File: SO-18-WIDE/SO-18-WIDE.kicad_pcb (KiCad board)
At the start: 2 copper layers, 3 parts

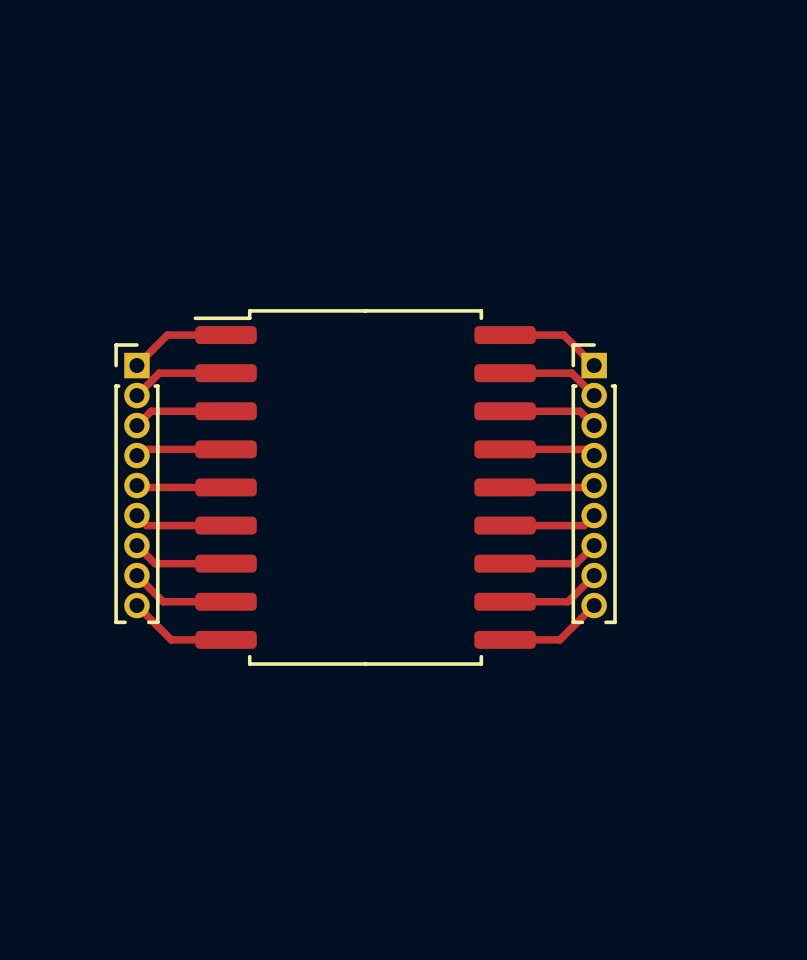
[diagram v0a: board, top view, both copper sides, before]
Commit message: added edge cuts
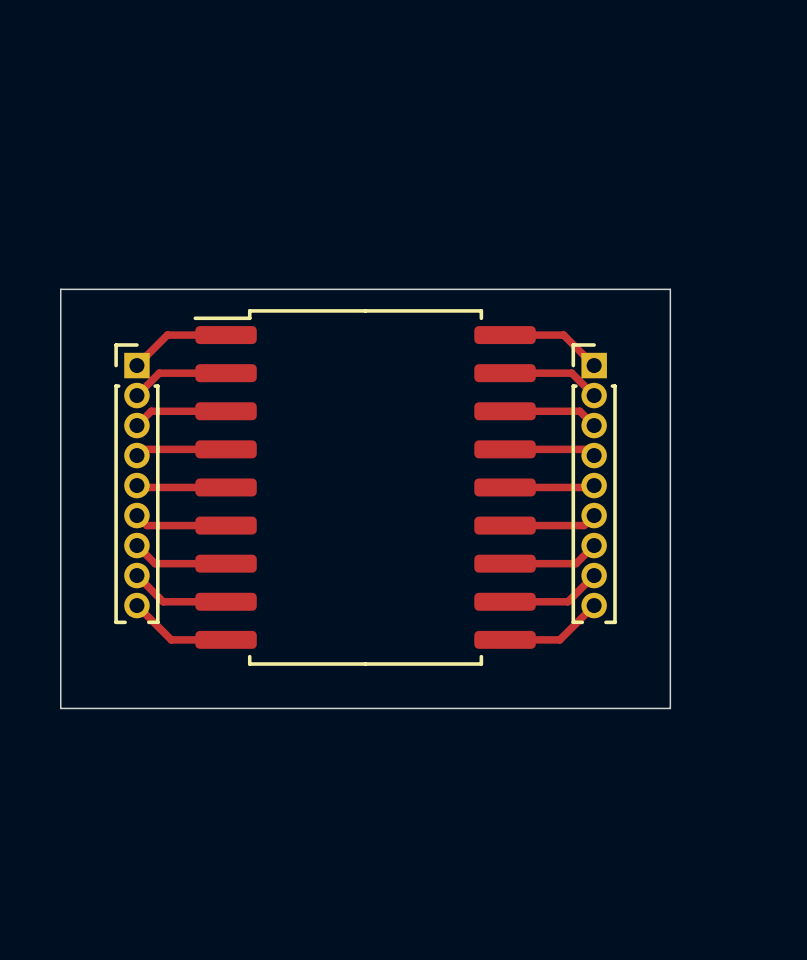
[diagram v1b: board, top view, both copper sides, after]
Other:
- board outline added: 20.3 x 14 mm
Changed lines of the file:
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@@
   (general
     (thickness 1.6)
-    (drawings 0)
+    (drawings 4)
     (tracks 36)
     (zones 0)
@@
     (pad_to_mask_clearance 0)
     (aux_axis_origin 0 0)
-    (visible_elements FFFFFF7F)
+    (visible_elements 7FFFFFFF)
     (pcbplotparams
       (layerselection 0x010fc_ffffffff)
@@
       (effects (font (size 1 1) (thickness 0.15)))
     )
+    (fp_line (start 1.15 -1) (end -1.15 -1) (layer F.CrtYd) (width 0.05))
+    (fp_line (start 1.15 9) (end 1.15 -1) (layer F.CrtYd) (width 0.05))
+    (fp_line (start -1.15 9) (end 1.15 9) (layer F.CrtYd) (width 0.05))
+    (fp_line (start -1.15 -1) (end -1.15 9) (layer F.CrtYd) (width 0.05))
+    (fp_line (start -0.695 -0.685) (end 0 -0.685) (layer F.SilkS) (width 0.12))
+    (fp_line (start -0.695 0) (end -0.695 -0.685) (layer F.SilkS) (width 0.12))
+    (fp_line (start 0.608276 0.685) (end 0.695 0.685) (layer F.SilkS) (width 0.12))
+    (fp_line (start -0.695 0.685) (end -0.608276 0.685) (layer F.SilkS) (width 0.12))
+    (fp_line (start 0.695 0.685) (end 0.695 8.56) (layer F.SilkS) (width 0.12))
+    (fp_line (start -0.695 0.685) (end -0.695 8.56) (layer F.SilkS) (width 0.12))
+    (fp_line (start 0.394493 8.56) (end 0.695 8.56) (layer F.SilkS) (width 0.12))
+    (fp_line (start -0.695 8.56) (end -0.394493 8.56) (layer F.SilkS) (width 0.12))
+    (fp_line (start -0.635 -0.1825) (end -0.3175 -0.5) (layer F.Fab) (width 0.1))
+    (fp_line (start -0.635 8.5) (end -0.635 -0.1825) (layer F.Fab) (width 0.1))
+    (fp_line (start 0.635 8.5) (end -0.635 8.5) (layer F.Fab) (width 0.1))
+    (fp_line (start 0.635 -0.5) (end 0.635 8.5) (layer F.Fab) (width 0.1))
     (fp_line (start -0.3175 -0.5) (end 0.635 -0.5) (layer F.Fab) (width 0.1))
-    (fp_line (start 0.635 -0.5) (end 0.635 8.5) (layer F.Fab) (width 0.1))
-    (fp_line (start 0.635 8.5) (end -0.635 8.5) (layer F.Fab) (width 0.1))
-    (fp_line (start -0.635 8.5) (end -0.635 -0.1825) (layer F.Fab) (width 0.1))
-    (fp_line (start -0.635 -0.1825) (end -0.3175 -0.5) (layer F.Fab) (width 0.1))
-    (fp_line (start -0.695 8.56) (end -0.394493 8.56) (layer F.SilkS) (width 0.12))
-    (fp_line (start 0.394493 8.56) (end 0.695 8.56) (layer F.SilkS) (width 0.12))
-    (fp_line (start -0.695 0.685) (end -0.695 8.56) (layer F.SilkS) (width 0.12))
-    (fp_line (start 0.695 0.685) (end 0.695 8.56) (layer F.SilkS) (width 0.12))
-    (fp_line (start -0.695 0.685) (end -0.608276 0.685) (layer F.SilkS) (width 0.12))
-    (fp_line (start 0.608276 0.685) (end 0.695 0.685) (layer F.SilkS) (width 0.12))
-    (fp_line (start -0.695 0) (end -0.695 -0.685) (layer F.SilkS) (width 0.12))
-    (fp_line (start -0.695 -0.685) (end 0 -0.685) (layer F.SilkS) (width 0.12))
-    (fp_line (start -1.15 -1) (end -1.15 9) (layer F.CrtYd) (width 0.05))
-    (fp_line (start -1.15 9) (end 1.15 9) (layer F.CrtYd) (width 0.05))
-    (fp_line (start 1.15 9) (end 1.15 -1) (layer F.CrtYd) (width 0.05))
-    (fp_line (start 1.15 -1) (end -1.15 -1) (layer F.CrtYd) (width 0.05))
     (fp_text user %R (at 0 4 90) (layer F.Fab)
       (effects (font (size 0.76 0.76) (thickness 0.114)))
@@
       (effects (font (size 1 1) (thickness 0.15)))
     )
+    (fp_line (start 1.15 -1) (end -1.15 -1) (layer F.CrtYd) (width 0.05))
+    (fp_line (start 1.15 9) (end 1.15 -1) (layer F.CrtYd) (width 0.05))
+    (fp_line (start -1.15 9) (end 1.15 9) (layer F.CrtYd) (width 0.05))
+    (fp_line (start -1.15 -1) (end -1.15 9) (layer F.CrtYd) (width 0.05))
+    (fp_line (start -0.695 -0.685) (end 0 -0.685) (layer F.SilkS) (width 0.12))
+    (fp_line (start -0.695 0) (end -0.695 -0.685) (layer F.SilkS) (width 0.12))
+    (fp_line (start 0.608276 0.685) (end 0.695 0.685) (layer F.SilkS) (width 0.12))
+    (fp_line (start -0.695 0.685) (end -0.608276 0.685) (layer F.SilkS) (width 0.12))
+    (fp_line (start 0.695 0.685) (end 0.695 8.56) (layer F.SilkS) (width 0.12))
+    (fp_line (start -0.695 0.685) (end -0.695 8.56) (layer F.SilkS) (width 0.12))
+    (fp_line (start 0.394493 8.56) (end 0.695 8.56) (layer F.SilkS) (width 0.12))
+    (fp_line (start -0.695 8.56) (end -0.394493 8.56) (layer F.SilkS) (width 0.12))
+    (fp_line (start -0.635 -0.1825) (end -0.3175 -0.5) (layer F.Fab) (width 0.1))
+    (fp_line (start -0.635 8.5) (end -0.635 -0.1825) (layer F.Fab) (width 0.1))
+    (fp_line (start 0.635 8.5) (end -0.635 8.5) (layer F.Fab) (width 0.1))
+    (fp_line (start 0.635 -0.5) (end 0.635 8.5) (layer F.Fab) (width 0.1))
+    (fp_line (start -0.3175 -0.5) (end 0.635 -0.5) (layer F.Fab) (width 0.1))
     (fp_text user %R (at 0 4 90) (layer F.Fab)
       (effects (font (size 0.76 0.76) (thickness 0.114)))
     )
-    (fp_line (start -0.3175 -0.5) (end 0.635 -0.5) (layer F.Fab) (width 0.1))
-    (fp_line (start 0.635 -0.5) (end 0.635 8.5) (layer F.Fab) (width 0.1))
-    (fp_line (start 0.635 8.5) (end -0.635 8.5) (layer F.Fab) (width 0.1))
-    (fp_line (start -0.635 8.5) (end -0.635 -0.1825) (layer F.Fab) (width 0.1))
-    (fp_line (start -0.635 -0.1825) (end -0.3175 -0.5) (layer F.Fab) (width 0.1))
-    (fp_line (start -0.695 8.56) (end -0.394493 8.56) (layer F.SilkS) (width 0.12))
-    (fp_line (start 0.394493 8.56) (end 0.695 8.56) (layer F.SilkS) (width 0.12))
-    (fp_line (start -0.695 0.685) (end -0.695 8.56) (layer F.SilkS) (width 0.12))
-    (fp_line (start 0.695 0.685) (end 0.695 8.56) (layer F.SilkS) (width 0.12))
-    (fp_line (start -0.695 0.685) (end -0.608276 0.685) (layer F.SilkS) (width 0.12))
-    (fp_line (start 0.608276 0.685) (end 0.695 0.685) (layer F.SilkS) (width 0.12))
-    (fp_line (start -0.695 0) (end -0.695 -0.685) (layer F.SilkS) (width 0.12))
-    (fp_line (start -0.695 -0.685) (end 0 -0.685) (layer F.SilkS) (width 0.12))
-    (fp_line (start -1.15 -1) (end -1.15 9) (layer F.CrtYd) (width 0.05))
-    (fp_line (start -1.15 9) (end 1.15 9) (layer F.CrtYd) (width 0.05))
-    (fp_line (start 1.15 9) (end 1.15 -1) (layer F.CrtYd) (width 0.05))
-    (fp_line (start 1.15 -1) (end -1.15 -1) (layer F.CrtYd) (width 0.05))
     (pad 9 thru_hole oval (at 0 8) (size 0.85 0.85) (drill 0.5) (layers *.Cu *.Mask))
     (pad 8 thru_hole oval (at 0 7) (size 0.85 0.85) (drill 0.5) (layers *.Cu *.Mask))
@@
       (effects (font (size 1 1) (thickness 0.15)))
     )
+    (fp_line (start 5.93 -6.02) (end -5.93 -6.02) (layer F.CrtYd) (width 0.05))
+    (fp_line (start 5.93 6.02) (end 5.93 -6.02) (layer F.CrtYd) (width 0.05))
+    (fp_line (start -5.93 6.02) (end 5.93 6.02) (layer F.CrtYd) (width 0.05))
+    (fp_line (start -5.93 -6.02) (end -5.93 6.02) (layer F.CrtYd) (width 0.05))
+    (fp_line (start -3.75 -4.775) (end -2.75 -5.775) (layer F.Fab) (width 0.1))
+    (fp_line (start -3.75 5.775) (end -3.75 -4.775) (layer F.Fab) (width 0.1))
+    (fp_line (start 3.75 5.775) (end -3.75 5.775) (layer F.Fab) (width 0.1))
+    (fp_line (start 3.75 -5.775) (end 3.75 5.775) (layer F.Fab) (width 0.1))
+    (fp_line (start -2.75 -5.775) (end 3.75 -5.775) (layer F.Fab) (width 0.1))
+    (fp_line (start -3.86 -5.64) (end -5.675 -5.64) (layer F.SilkS) (width 0.12))
+    (fp_line (start -3.86 -5.885) (end -3.86 -5.64) (layer F.SilkS) (width 0.12))
+    (fp_line (start 0 -5.885) (end -3.86 -5.885) (layer F.SilkS) (width 0.12))
+    (fp_line (start 3.86 -5.885) (end 3.86 -5.64) (layer F.SilkS) (width 0.12))
+    (fp_line (start 0 -5.885) (end 3.86 -5.885) (layer F.SilkS) (width 0.12))
+    (fp_line (start -3.86 5.885) (end -3.86 5.64) (layer F.SilkS) (width 0.12))
+    (fp_line (start 0 5.885) (end -3.86 5.885) (layer F.SilkS) (width 0.12))
+    (fp_line (start 3.86 5.885) (end 3.86 5.64) (layer F.SilkS) (width 0.12))
+    (fp_line (start 0 5.885) (end 3.86 5.885) (layer F.SilkS) (width 0.12))
     (fp_text user %R (at 0 0) (layer F.Fab)
       (effects (font (size 1 1) (thickness 0.15)))
     )
-    (fp_line (start 0 5.885) (end 3.86 5.885) (layer F.SilkS) (width 0.12))
-    (fp_line (start 3.86 5.885) (end 3.86 5.64) (layer F.SilkS) (width 0.12))
-    (fp_line (start 0 5.885) (end -3.86 5.885) (layer F.SilkS) (width 0.12))
-    (fp_line (start -3.86 5.885) (end -3.86 5.64) (layer F.SilkS) (width 0.12))
-    (fp_line (start 0 -5.885) (end 3.86 -5.885) (layer F.SilkS) (width 0.12))
-    (fp_line (start 3.86 -5.885) (end 3.86 -5.64) (layer F.SilkS) (width 0.12))
-    (fp_line (start 0 -5.885) (end -3.86 -5.885) (layer F.SilkS) (width 0.12))
-    (fp_line (start -3.86 -5.885) (end -3.86 -5.64) (layer F.SilkS) (width 0.12))
-    (fp_line (start -3.86 -5.64) (end -5.675 -5.64) (layer F.SilkS) (width 0.12))
-    (fp_line (start -2.75 -5.775) (end 3.75 -5.775) (layer F.Fab) (width 0.1))
-    (fp_line (start 3.75 -5.775) (end 3.75 5.775) (layer F.Fab) (width 0.1))
-    (fp_line (start 3.75 5.775) (end -3.75 5.775) (layer F.Fab) (width 0.1))
-    (fp_line (start -3.75 5.775) (end -3.75 -4.775) (layer F.Fab) (width 0.1))
-    (fp_line (start -3.75 -4.775) (end -2.75 -5.775) (layer F.Fab) (width 0.1))
-    (fp_line (start -5.93 -6.02) (end -5.93 6.02) (layer F.CrtYd) (width 0.05))
-    (fp_line (start -5.93 6.02) (end 5.93 6.02) (layer F.CrtYd) (width 0.05))
-    (fp_line (start 5.93 6.02) (end 5.93 -6.02) (layer F.CrtYd) (width 0.05))
-    (fp_line (start 5.93 -6.02) (end -5.93 -6.02) (layer F.CrtYd) (width 0.05))
     (pad 18 smd roundrect (at 4.65 -5.08) (size 2.05 0.6) (layers F.Cu F.Paste F.Mask) (roundrect_rratio 0.25))
     (pad 17 smd roundrect (at 4.65 -3.81) (size 2.05 0.6) (layers F.Cu F.Paste F.Mask) (roundrect_rratio 0.25))
@@
     )
   )
+  (gr_line (start 142.24 90.17) (end 121.92 90.17) (layer Edge.Cuts) (width 0.05))
+  (gr_line (start 142.24 76.2) (end 142.24 90.17) (layer Edge.Cuts) (width 0.05))
+  (gr_line (start 121.92 76.2) (end 142.24 76.2) (layer Edge.Cuts) (width 0.05))
+  (gr_line (start 121.92 90.17) (end 121.92 76.2) (layer Edge.Cuts) (width 0.05))
   (segment (start 138.684 77.724) (end 139.7 78.74) (width 0.25) (layer F.Cu) (net 0))
   (segment (start 136.73 77.724) (end 138.684 77.724) (width 0.25) (layer F.Cu) (net 0))

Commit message: changed headers to 2.54
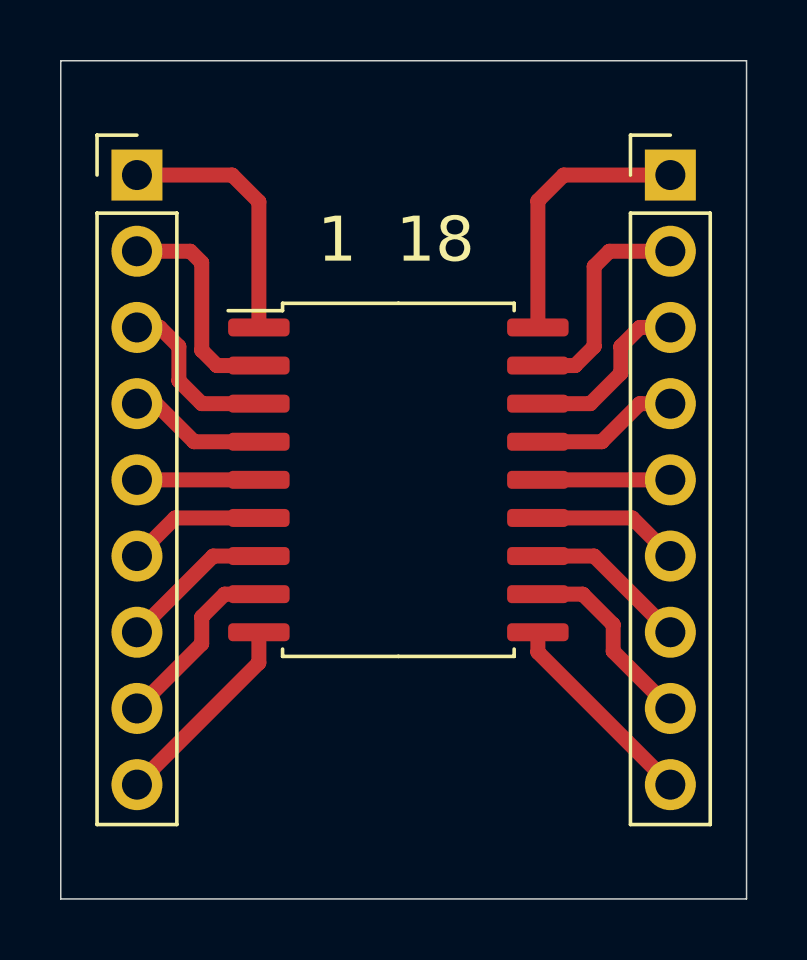
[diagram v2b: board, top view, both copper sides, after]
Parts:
- removed the REF** at (139.7, 78.7)
- removed the REF** at (124.5, 78.7)
- added REF**: PinHeader_1x09_P2.54mm_Vertical, Connector_PinHeader_2.54mm:PinHeader_1x09_P2.54mm_Vertical, F.Cu at (142.2, 72.4)
- added REF**: PinHeader_1x09_P2.54mm_Vertical, Connector_PinHeader_2.54mm:PinHeader_1x09_P2.54mm_Vertical, F.Cu at (124.5, 72.4)
- moved REF** 1.12 mm to (133.2, 82.5)
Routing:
- net (no net): track 58.0 -> 108.8 mm
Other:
- board size 20.3 x 14 mm -> 22.9 x 27.9 mm
- board text added: "1 18"
